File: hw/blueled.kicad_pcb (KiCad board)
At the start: 2 copper layers, 54 x 85.6 mm, 59 parts, among them J1 Barrel_Jack, J2 LED Strip, J3 ICSP, J4 Screw_Terminal_01x02, Q1 Q_PMOS_SDG, Q2 Q_PNP_EBC, SW2 PUSH, U1 ATmega328P-AU, U2 HC-05, U3 AMS1117-3.3, U4 AT25SF081, U5 LM25085MM, X1 CSTCE

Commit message: add(hw): level shifter + layout progress
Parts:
- turned C9 to 270 degrees
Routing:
- net +5V: track 22.2 -> 164.1 mm, vias 27 -> 32
- net Net-(C9-Pad2): track 9.95 -> 60.4 mm, vias 0 -> 2
- net +3V3: track 92.9 -> 108.0 mm
- added copper zone on F.Cu, net Net-(D5-Pad1)
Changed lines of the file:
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@@
     (thickness 1.6)
     (drawings 9)
-    (tracks 296)
+    (tracks 347)
     (zones 0)
     (modules 59)
@@
     (tags "capacitor tantalum")
     (attr smd)
-    (fp_text reference C1 (at 4 0) (layer F.SilkS)
+    (fp_text reference C1 (at -4 0) (layer F.SilkS)
       (effects (font (size 1 1) (thickness 0.15)))
     )
@@
   )
   (module Capacitor_SMD:C_0805_2012Metric_Pad1.15x1.40mm_HandSolder (layer F.Cu)
-    (at 135.55 91.46 90)
+    (at 135.55 91.46 270)
     (descr "Capacitor SMD 0805 (2012 Metric), square (rectangular) end terminal, IPC_7351 nominal with elongated pad for handsoldering. (Body size source: https://docs.google.com/spreadsheets/d/1BsfQQcO9C6DZCsRaXUlFlo91Tg2WpOkGARC1WS5S8t0/edit?usp=sharing), generated with kicad-footprint-generator")
     (tags "capacitor handsolder")
     (attr smd)
-    (fp_text reference C9 (at -3.04 -0.05 90) (layer F.SilkS)
+    (fp_text reference C9 (at 3.04 -0.05 90) (layer F.SilkS)
       (effects (font (size 1 1) (thickness 0.15)))
     )
@@
       (effects (font (size 0.5 0.5) (thickness 0.08)))
     )
-    (pad 2 smd roundrect (at 1.025 0 90) (size 1.15 1.4) (layers F.Cu F.Paste F.Mask) (roundrect_rratio 0.217391)
+    (pad 2 smd roundrect (at 1.025 0 270) (size 1.15 1.4) (layers F.Cu F.Paste F.Mask) (roundrect_rratio 0.217391)
       (net 30 "Net-(C9-Pad2)"))
-    (pad 1 smd roundrect (at -1.025 0 90) (size 1.15 1.4) (layers F.Cu F.Paste F.Mask) (roundrect_rratio 0.217391)
+    (pad 1 smd roundrect (at -1.025 0 270) (size 1.15 1.4) (layers F.Cu F.Paste F.Mask) (roundrect_rratio 0.217391)
       (net 27 +5V))
     (model ${KISYS3DMOD}/Capacitor_SMD.3dshapes/C_0805_2012Metric.wrl
@@
   (segment (start 162.433265 91.11) (end 165.5 91.11) (width 0.5) (layer B.Cu) (net 24))
   (via (at 165.5 91.11) (size 0.8) (drill 0.4) (layers F.Cu B.Cu) (net 24))
+  (segment (start 151.780754 114.95001) (end 146.525 109.694256) (width 0.5) (layer F.Cu) (net 24))
+  (segment (start 153.119266 114.95001) (end 151.780754 114.95001) (width 0.5) (layer F.Cu) (net 24))
+  (segment (start 153.60001 115.430754) (end 153.119266 114.95001) (width 0.5) (layer F.Cu) (net 24))
+  (segment (start 153.60001 119.21999) (end 153.60001 115.430754) (width 0.5) (layer F.Cu) (net 24))
+  (segment (start 146.525 109.694256) (end 146.525 108.5) (width 0.5) (layer F.Cu) (net 24))
+  (segment (start 153.15 119.67) (end 153.60001 119.21999) (width 0.5) (layer F.Cu) (net 24))
   (segment (start 135.475 78) (end 134 79.475) (width 0.5) (layer F.Cu) (net 27))
   (segment (start 134 79.475) (end 134 82) (width 0.5) (layer F.Cu) (net 27))
@@
   (segment (start 142 70.08) (end 141.42 69.5) (width 2.5) (layer F.Cu) (net 27))
   (segment (start 142 81) (end 142 70.08) (width 2.5) (layer F.Cu) (net 27))
+  (segment (start 146.9375 113.3875) (end 144.35 110.8) (width 0.5) (layer F.Cu) (net 27))
+  (segment (start 146.9375 114) (end 146.9375 113.3875) (width 0.5) (layer F.Cu) (net 27))
+  (segment (start 144.95 94) (end 144.95 94.45) (width 0.5) (layer F.Cu) (net 27))
+  (segment (start 144.95 94.45) (end 146 95.5) (width 0.5) (layer F.Cu) (net 27))
+  (via (at 146 95.5) (size 0.8) (drill 0.4) (layers F.Cu B.Cu) (net 27))
+  (segment (start 146 95.5) (end 146 91) (width 0.5) (layer B.Cu) (net 27))
+  (segment (start 146 91) (end 149.5 87.5) (width 0.5) (layer B.Cu) (net 27))
+  (via (at 149.5 87.5) (size 0.8) (drill 0.4) (layers F.Cu B.Cu) (net 27))
+  (segment (start 150.58 87.5) (end 150.67 87.41) (width 0.5) (layer F.Cu) (net 27))
+  (segment (start 149.5 87.5) (end 150.58 87.5) (width 0.5) (layer F.Cu) (net 27))
+  (segment (start 133.15 88.035) (end 134.5575 89.4425) (width 0.5) (layer F.Cu) (net 27))
+  (segment (start 133.15 82.85) (end 133.15 88.035) (width 0.5) (layer F.Cu) (net 27))
+  (segment (start 134.5575 89.4425) (end 135.55 90.435) (width 0.5) (layer F.Cu) (net 27))
+  (via (at 134.5575 89.4425) (size 0.8) (drill 0.4) (layers F.Cu B.Cu) (net 27))
+  (segment (start 145.199999 94.699999) (end 146 95.5) (width 0.5) (layer B.Cu) (net 27))
+  (segment (start 139.814999 94.699999) (end 145.199999 94.699999) (width 0.5) (layer B.Cu) (net 27))
+  (segment (start 134.5575 89.4425) (end 139.814999 94.699999) (width 0.5) (layer B.Cu) (net 27))
+  (segment (start 146 94.934315) (end 146 95.5) (width 1.5) (layer B.Cu) (net 27))
+  (segment (start 145.265684 94.199999) (end 146 94.934315) (width 1.5) (layer B.Cu) (net 27))
+  (segment (start 142.275997 94.199999) (end 145.265684 94.199999) (width 1.5) (layer B.Cu) (net 27))
+  (segment (start 133 84.924002) (end 142.275997 94.199999) (width 1.5) (layer B.Cu) (net 27))
+  (segment (start 133 80) (end 133 84.924002) (width 1.5) (layer B.Cu) (net 27))
+  (segment (start 146 95.5) (end 146 111) (width 1.5) (layer B.Cu) (net 27))
+  (segment (start 146 111) (end 146.25 111.25) (width 1.5) (layer B.Cu) (net 27))
+  (segment (start 147 112) (end 147 112) (width 1.5) (layer B.Cu) (net 27))
+  (via (at 147 112) (size 0.8) (drill 0.4) (layers F.Cu B.Cu) (net 27))
+  (segment (start 146.25 111.25) (end 147 112) (width 1.5) (layer B.Cu) (net 27))
+  (via (at 146.25 111.25) (size 0.8) (drill 0.4) (layers F.Cu B.Cu) (net 27))
+  (segment (start 145.8 110.8) (end 144.35 110.8) (width 1.5) (layer F.Cu) (net 27))
+  (segment (start 147 112) (end 145.8 110.8) (width 1.5) (layer F.Cu) (net 27))
+  (segment (start 124 80) (end 121.5 80) (width 0.5) (layer F.Cu) (net 27))
+  (segment (start 121.5 80) (end 121 80.5) (width 0.5) (layer F.Cu) (net 27))
+  (segment (start 121 130.125) (end 125.905 135.03) (width 0.5) (layer F.Cu) (net 27))
+  (segment (start 121 80.5) (end 121 130.125) (width 0.5) (layer F.Cu) (net 27))
   (segment (start 154.1375 127.7) (end 156.5 127.7) (width 0.5) (layer F.Cu) (net 28))
   (segment (start 152.5 126.0625) (end 154.1375 127.7) (width 0.5) (layer F.Cu) (net 28))
@@
   (segment (start 135.955 127.111004) (end 135.955 124.03) (width 0.5) (layer F.Cu) (net 29))
   (segment (start 133.976001 128.070001) (end 134.996003 128.070001) (width 0.5) (layer F.Cu) (net 29))
-  (segment (start 130.596003 128.720001) (end 129.576001 128.720001) (width 0.5) (layer F.Cu) (net 30))
   (segment (start 130.701002 128.825) (end 130.596003 128.720001) (width 0.5) (layer F.Cu) (net 30))
   (segment (start 127.955 135.03) (end 130.405 135.03) (width 0.5) (layer F.Cu) (net 30))
+  (segment (start 130.405 135.03) (end 130.701002 134.733998) (width 0.5) (layer F.Cu) (net 30))
+  (segment (start 135.55 92.485) (end 135.55 93.05) (width 0.5) (layer F.Cu) (net 30))
+  (segment (start 135.55 93.05) (end 136.5 94) (width 0.5) (layer F.Cu) (net 30))
+  (via (at 136.5 94) (size 0.8) (drill 0.4) (layers F.Cu B.Cu) (net 30))
+  (segment (start 136.5 94) (end 136.5 99) (width 0.5) (layer B.Cu) (net 30))
+  (segment (start 136.5 99) (end 142 104.5) (width 0.5) (layer B.Cu) (net 30))
+  (segment (start 142 104.5) (end 142 122.5) (width 0.5) (layer B.Cu) (net 30))
   (segment (start 130.701002 134.733998) (end 130.701002 128.825) (width 0.5) (layer F.Cu) (net 30))
-  (segment (start 130.405 135.03) (end 130.701002 134.733998) (width 0.5) (layer F.Cu) (net 30))
+  (segment (start 142 122.5) (end 142 126.5) (width 0.5) (layer B.Cu) (net 30))
+  (segment (start 142 126.5) (end 138 130.5) (width 0.5) (layer B.Cu) (net 30))
+  (via (at 138 130.5) (size 0.8) (drill 0.4) (layers F.Cu B.Cu) (net 30))
+  (segment (start 130.596003 128.720001) (end 129.576001 128.720001) (width 0.5) (layer F.Cu) (net 30))
+  (segment (start 132.376002 130.5) (end 130.596003 128.720001) (width 0.5) (layer F.Cu) (net 30))
+  (segment (start 138 130.5) (end 132.376002 130.5) (width 0.5) (layer F.Cu) (net 30))
   (segment (start 135.5125 87.5) (end 135.5125 82.5) (width 0.5) (layer F.Cu) (net 31))
   (segment (start 135.5125 80.0125) (end 137.525 78) (width 0.5) (layer F.Cu) (net 31))
@@
       )
     )
+  )
+  (zone (net 34) (net_name "Net-(D5-Pad1)") (layer F.Cu) (hatch edge 0.508)
+    (connect_pads yes (clearance 0.254))
+    (min_thickness 0.254)
+    (fill (arc_segments 32) (thermal_gap 0.508) (thermal_bridge_width 0.508))
+    (polygon
+      (pts
+        (xy 132.5 93) (xy 135.5 99) (xy 141 104.5) (xy 141 118) (xy 134.5 118)
+        (xy 132.5 110.5) (xy 122 110.5) (xy 122 100) (xy 125 93) (xy 125 88.5)
+        (xy 132.5 88.5)
+      )
+    )

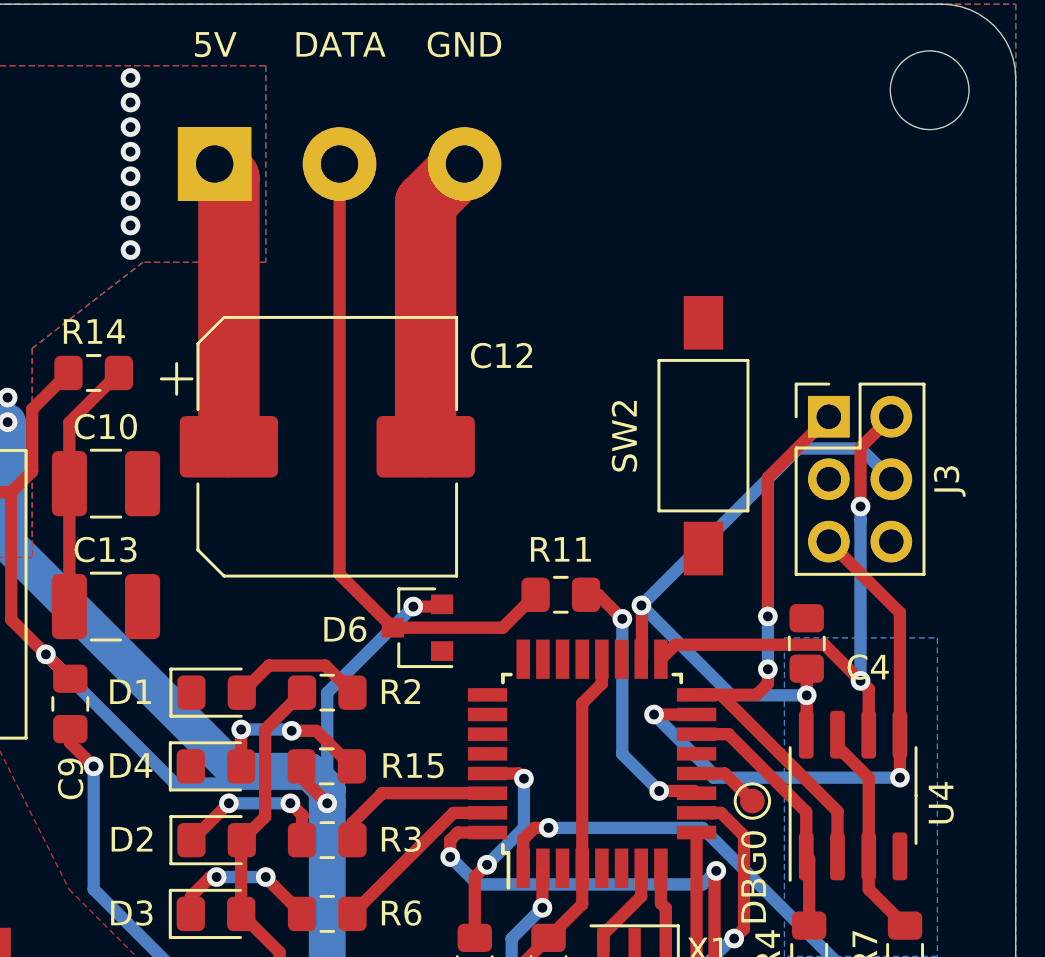
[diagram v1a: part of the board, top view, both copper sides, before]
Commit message: add(hw): routed level shifter
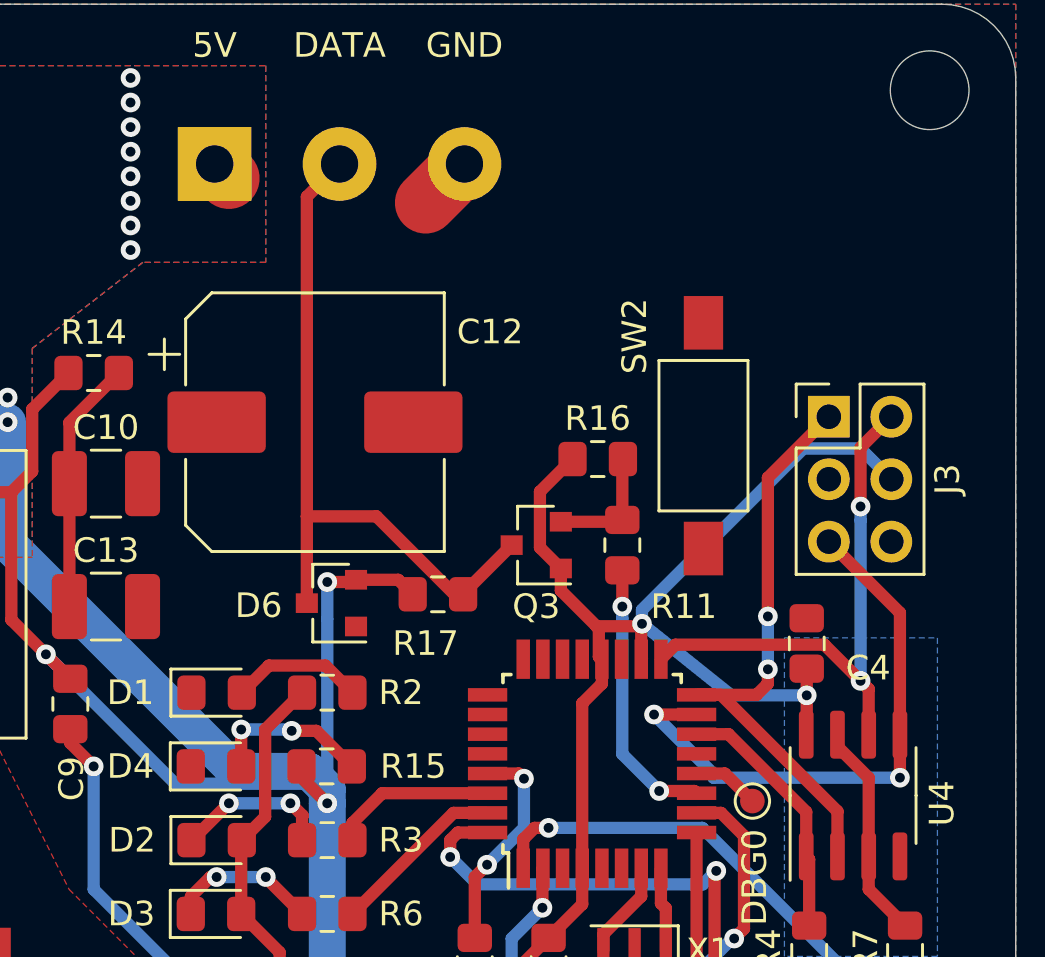
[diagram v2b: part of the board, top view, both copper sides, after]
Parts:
- added Q3: BSS138, Package_TO_SOT_SMD:SOT-23, F.Cu at (154.5, 85.0)
- added R16: 1k, Resistor_SMD:R_0805_2012Metric_Pad1.15x1.40mm_HandSolder, F.Cu at (157.0, 81.5)
- added R17: 1k, Resistor_SMD:R_0805_2012Metric_Pad1.15x1.40mm_HandSolder, F.Cu at (150.5, 87.0)
- moved D6 3.64 mm to (146.2, 87.4)
- moved R11 3.21 mm to (158.0, 85.0), turned to 90 degrees
- moved C12 1.12 mm to (145.5, 80.0)
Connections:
- R11 pad 2: /DATA -> Net-(Q3-Pad2)
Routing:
- net +3V3: track 108.0 -> 119.0 mm
- net GND: track 12.2 -> 2.23 mm
- net +5V: track 164.1 -> 155.1 mm
- net Net-(Q3-Pad2): track 0.00 -> 5.02 mm
- net /DATA: track 26.1 -> 28.9 mm

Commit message: add(hw): almost finished layout
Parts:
- JP1, JP2: moved to F.Cu
- moved JP2 29.3 mm to (154.0, 110.0), turned to 0 degrees
- moved JP1 28.6 mm to (154.0, 107.5)
- moved HRT1 8.93 mm to (171.5, 89.0)
- moved DBG1 1.88 mm to (149.9, 122.3)
- moved D5 1.27 mm to (129.0, 108.6)
- moved Q1 0.87 mm to (138.5, 116.5)
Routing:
- net /RESET: track 8.87 -> 28.8 mm, vias 2 -> 4
- net Net-(HRT1-Pad1): track 0.00 -> 19.7 mm, vias 0 -> 2
- net /RX: track 6.70 -> 21.9 mm, vias 0 -> 2
- net /TX: track 7.20 -> 21.3 mm, vias 0 -> 2
- net GND: track 2.23 -> 13.8 mm, vias 0 -> 43
- net +5V: track 155.1 -> 164.5 mm
- net Net-(Q1-Pad1): track 0.00 -> 7.83 mm
- net Net-(JP1-Pad2): track 0.00 -> 4.47 mm
- net +3V3: track 119.0 -> 122.8 mm
- net Net-(JP2-Pad2): track 0.00 -> 3.70 mm
- net Net-(C5-Pad1): track 8.41 -> 11.0 mm
- added copper zone on F.Cu, net /VINJACK
- added copper zone on F.Cu, net Net-(Q1-Pad1)
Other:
- board text added: "The connection for +5V has to be really big as it should withstand 5A"
- board text added: "The cut off region is for Bluetooth antena"
- board text added: "These arrays of vias are for thermal releaf"
- board text added: "This Region between D5, L1 and Q1 has to be large but not too large (EMI radiation)"

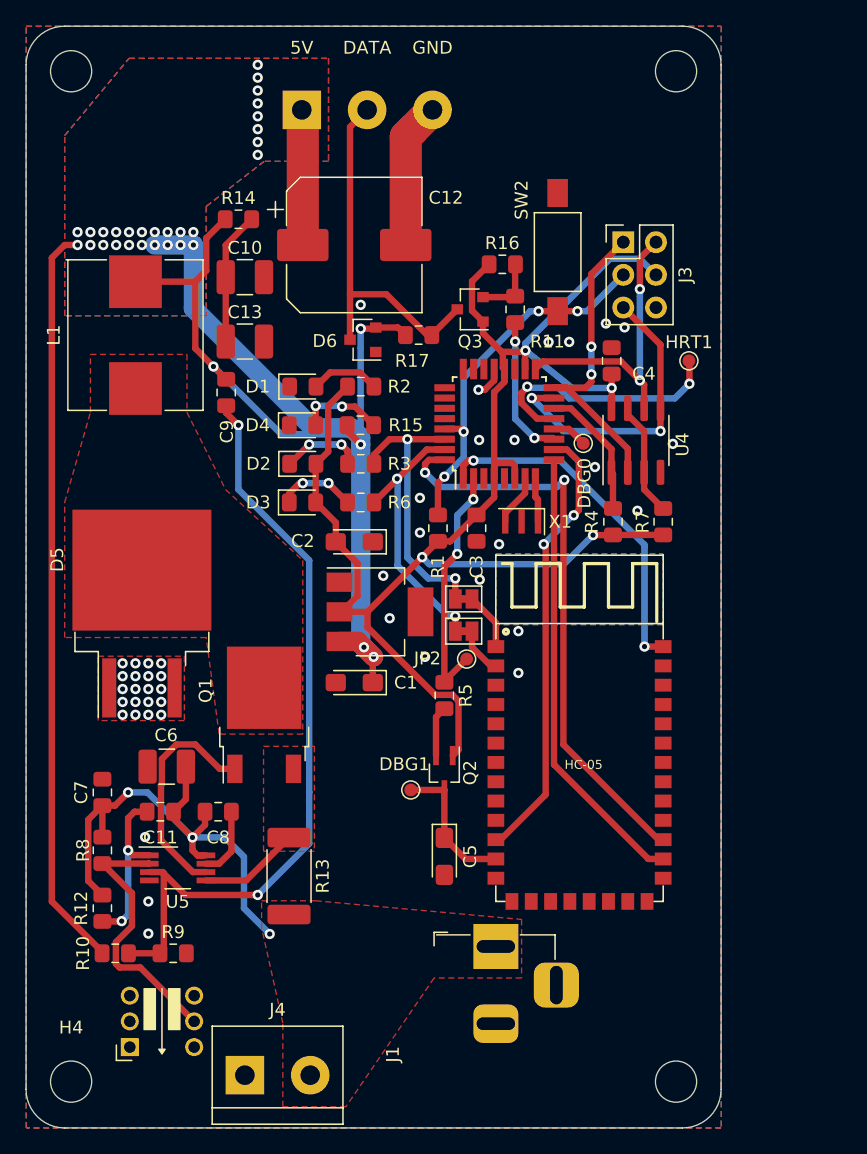
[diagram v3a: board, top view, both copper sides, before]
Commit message: add(hw): thermal vias and vias on high current traces
https://www.eevblog.com/forum/projects/via-stitching-for-high-current-traces/
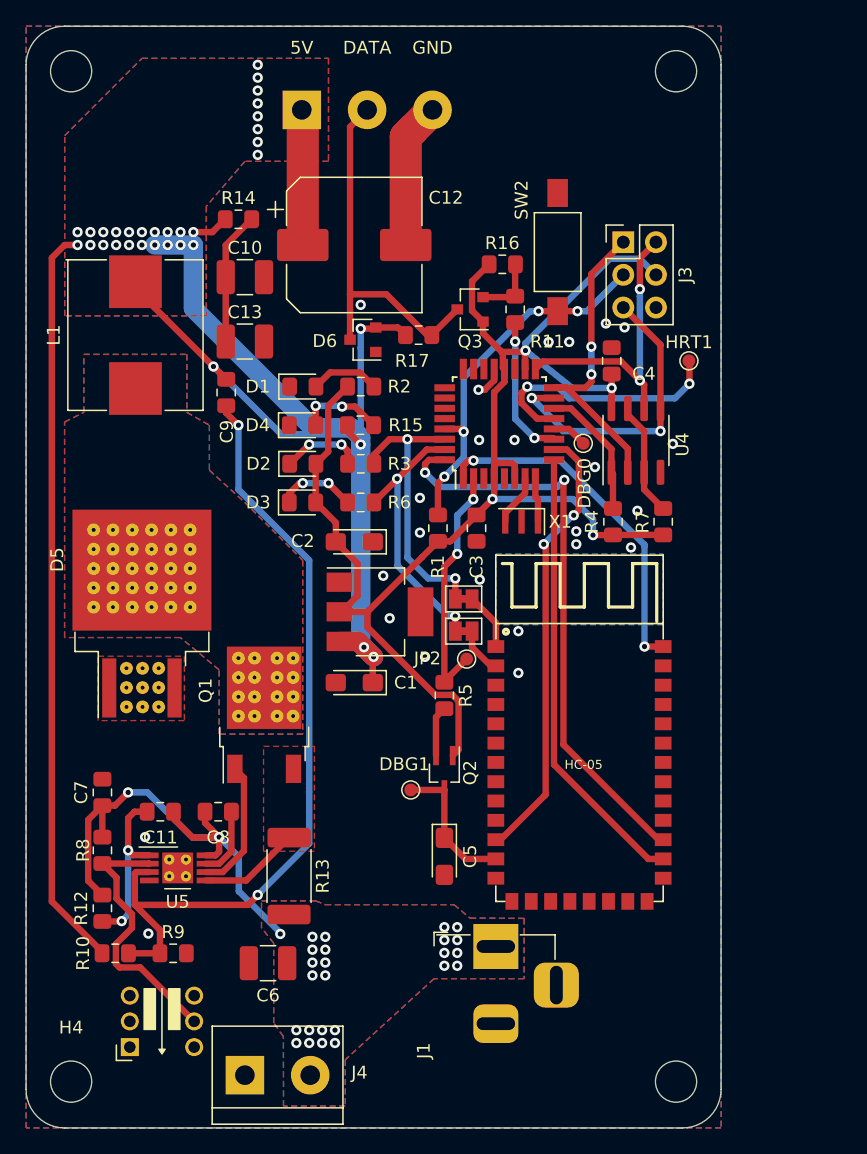
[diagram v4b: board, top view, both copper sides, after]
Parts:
- moved C6 17.2 mm to (138.8, 135.8)
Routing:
- net Net-(Q1-Pad3): track 17.8 -> 10.3 mm
- net +5V: track 164.5 -> 158.8 mm, vias 32 -> 33
- net +3V3: track 122.8 -> 118.0 mm
- net Net-(C9-Pad2): track 60.4 -> 63.3 mm
- net /VINJACK: track 41.8 -> 40.2 mm, vias 3 -> 27
- net GND: vias 43 -> 24
- net (no net): vias 1 -> 0
- added copper zone on B.Cu, net /VINJACK
- added copper zone on B.Cu, net Net-(D5-Pad1)

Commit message: fix(hw): just moved a label on silk screen
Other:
- board text added: "Blueled 01/01/2021 rev 2 alberand"
- board text removed: "Blueled 19/04/2020 rev 2 alberand"
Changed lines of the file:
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@@
   (gr_line (start 174 66) (end 174 145.6) (layer Edge.Cuts) (width 0.05))
   (gr_line (start 123 148.6) (end 171 148.6) (layer Edge.Cuts) (width 0.05))
-  (gr_text "Blueled\n19/04/2020 rev 2\nalberand" (at 145.4197 125.5395 90) (layer B.SilkS)
+  (gr_text "Blueled\n01/01/2021 rev 2\nalberand" (at 163.5 70.75) (layer B.SilkS)
     (effects (font (size 1 1) (thickness 0.15)) (justify mirror))
   )
